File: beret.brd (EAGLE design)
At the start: 65 x 56 mm, 0 parts

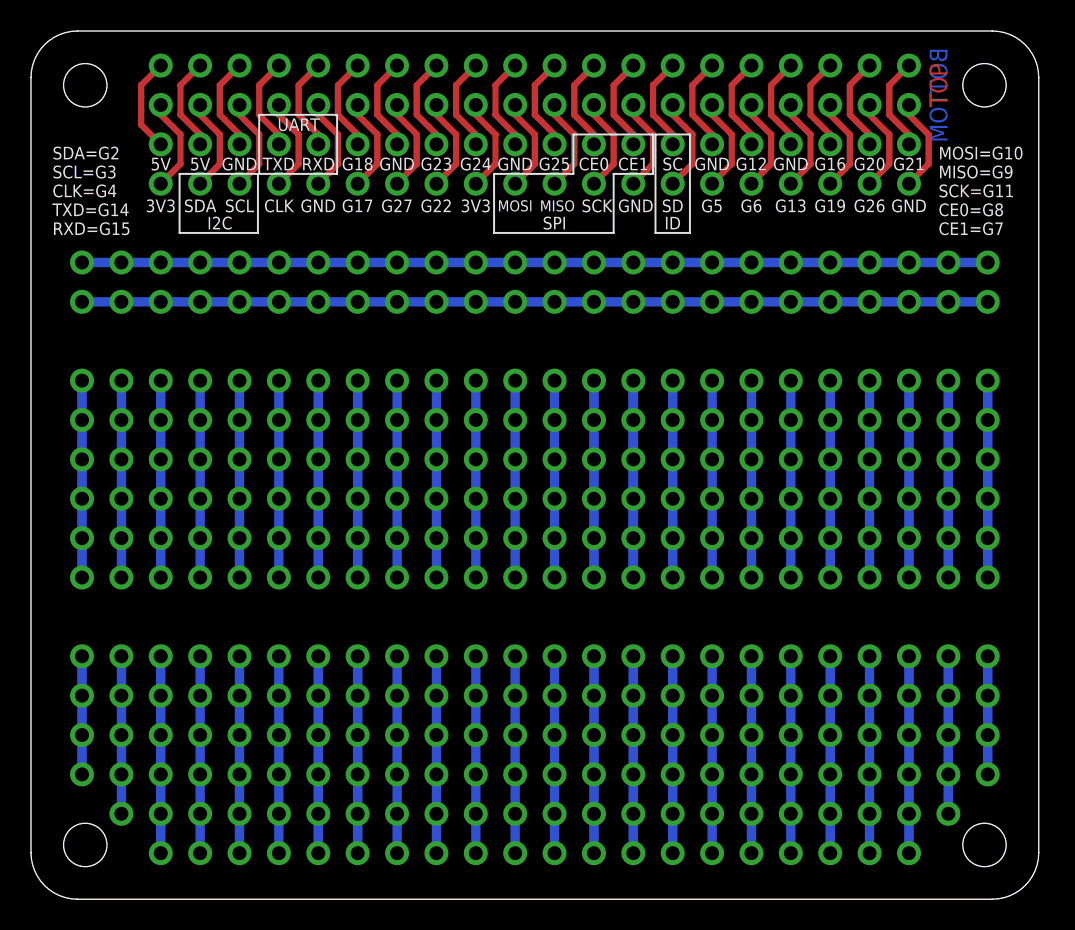
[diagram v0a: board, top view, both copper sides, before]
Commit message: Layout out for DroTek 10 DOF IMU + tweaks
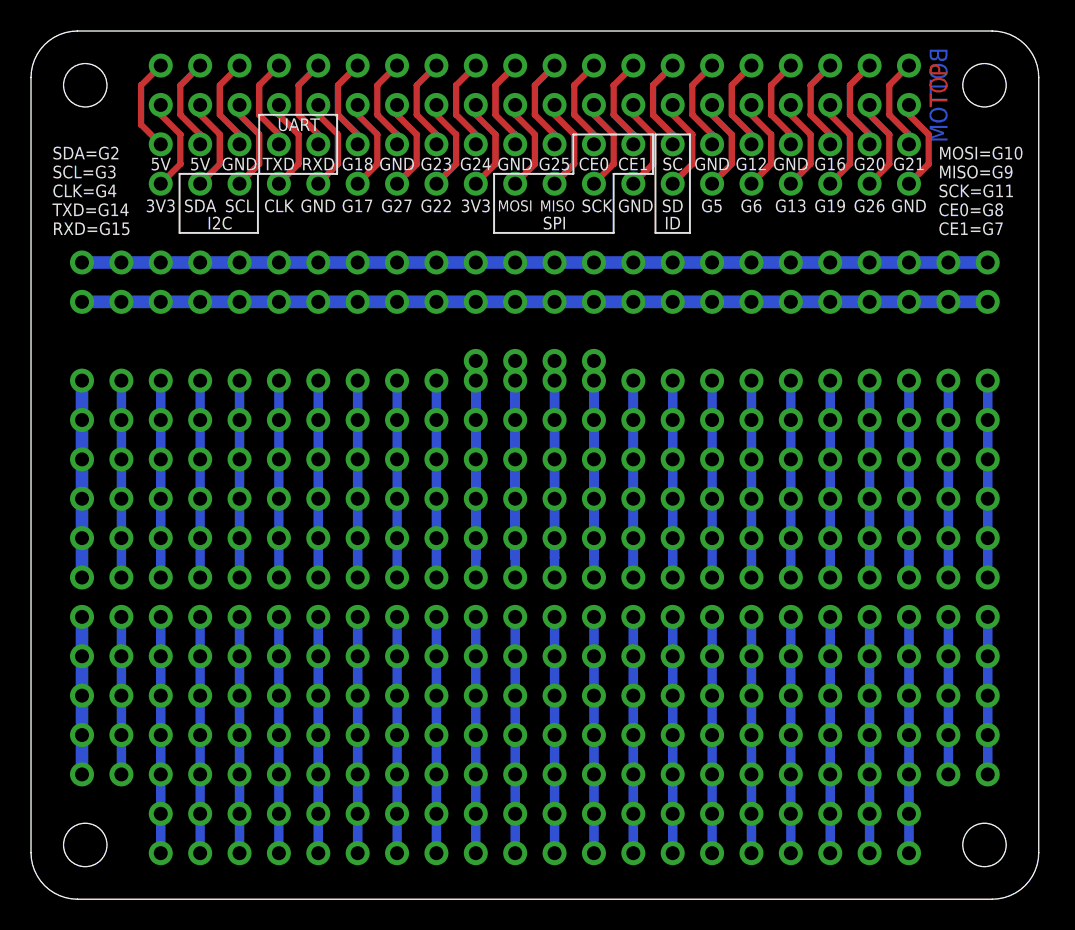
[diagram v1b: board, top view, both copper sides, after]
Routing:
- net S$42: track 304.8 -> 355.6 mm
- net S$41: track 302.3 -> 335.3 mm
- net S$212: track 0.00 -> 12.7 mm
- net S$164: track 0.00 -> 10.2 mm, vias 2 -> 4
